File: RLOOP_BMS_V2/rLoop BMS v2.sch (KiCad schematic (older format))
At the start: 0 parts

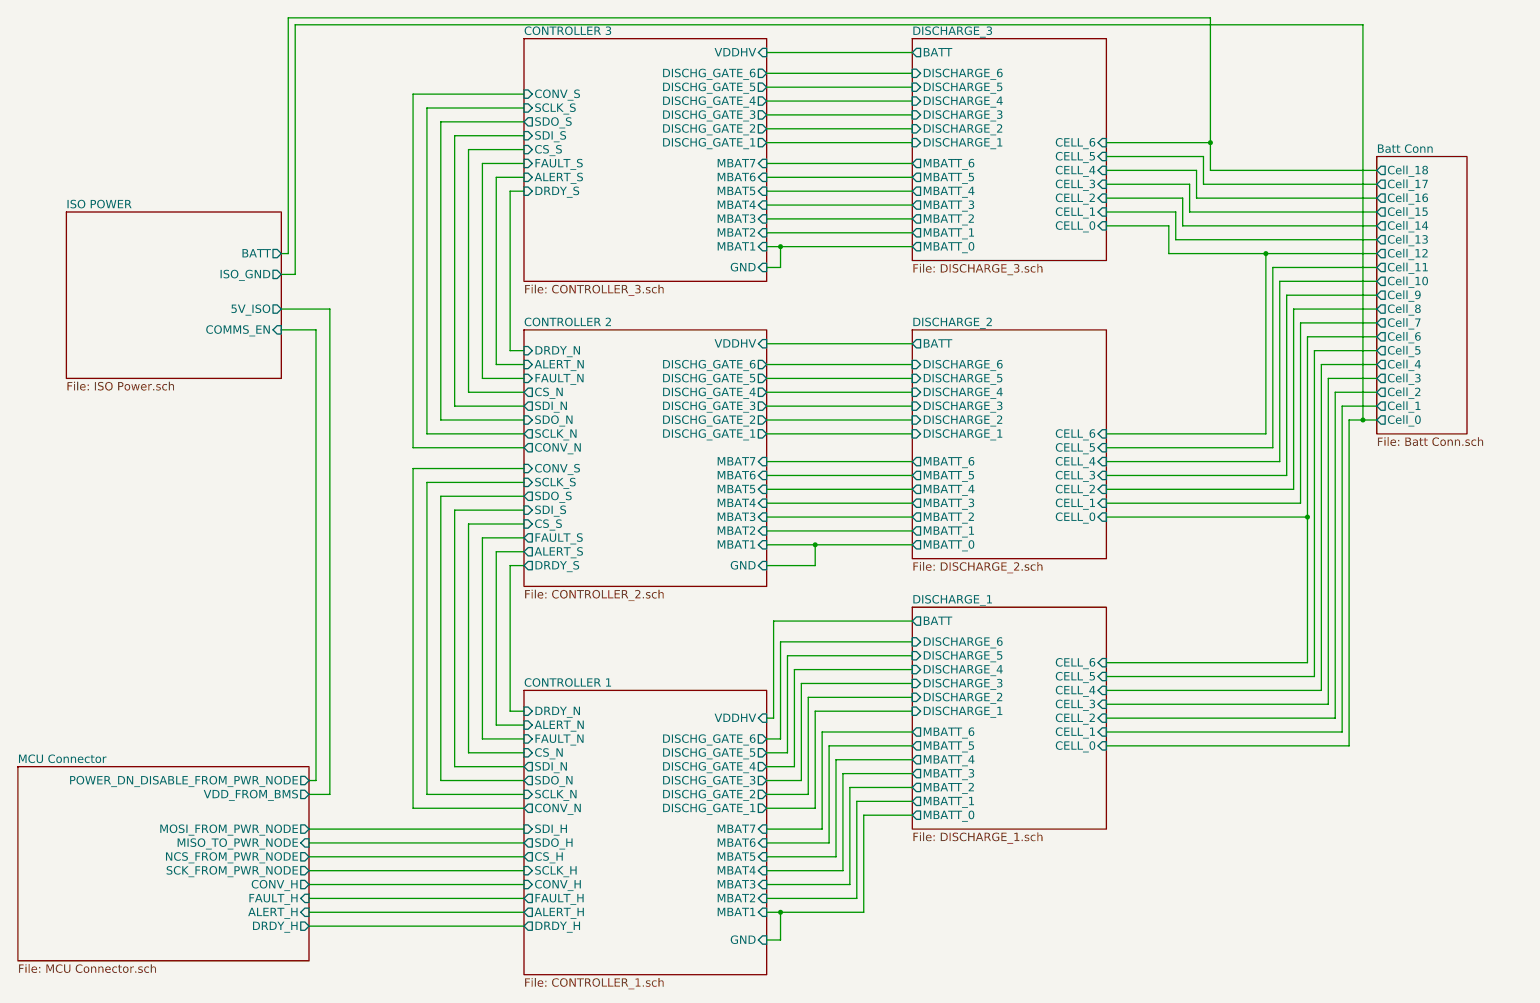
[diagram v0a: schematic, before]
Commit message: Updated page sizes for schematics
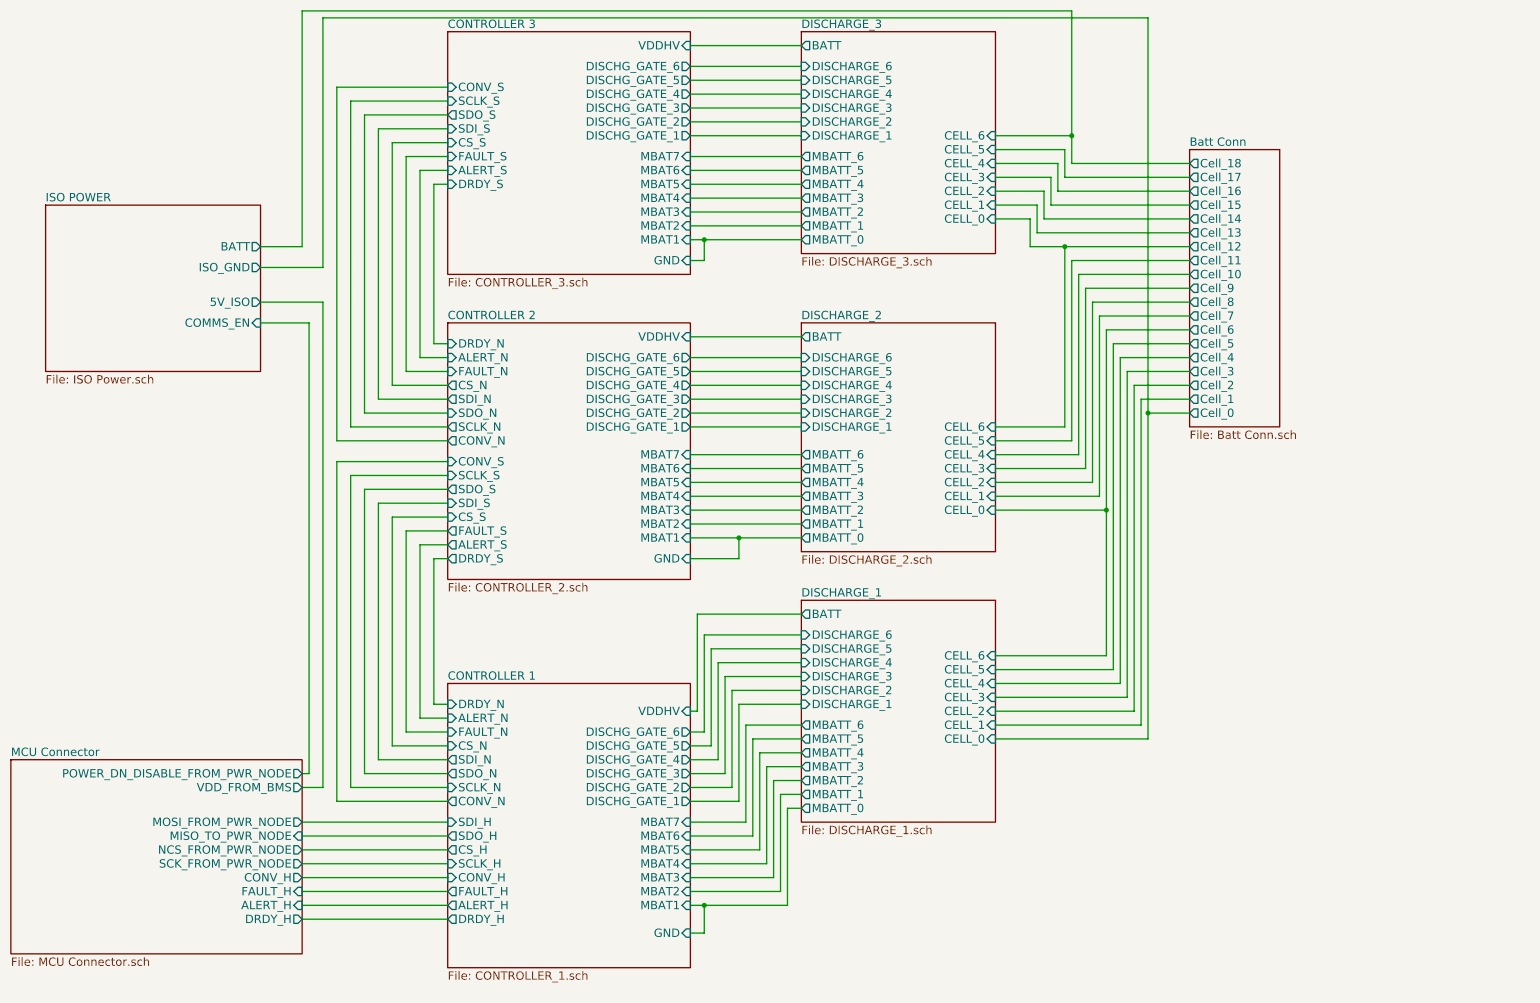
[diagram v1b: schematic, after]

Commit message: change Q1 transistor
Fixing something out of stock
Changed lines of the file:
@@
 	5450 2050 6250 2050
 Wire Wire Line
-	5450 2150 5550 2150
-Wire Wire Line
-	5550 2150 6250 2150
+	5450 2150 6250 2150
 Wire Wire Line
 	5450 2300 5550 2300
@@
 	5450 4200 6250 4200
 Wire Wire Line
-	5450 4300 5800 4300
-Wire Wire Line
-	5800 4300 6250 4300
+	5450 4300 6250 4300
 Wire Wire Line
 	5450 5550 5500 5550
@@
 	6150 6950 6150 6250
 Wire Wire Line
-	5450 6950 5550 6950
-Wire Wire Line
-	5550 6950 6150 6950
+	5450 6950 6150 6950
 Wire Wire Line
 	5450 7150 5550 7150
@@
 Connection ~ 5550 6950
 Wire Wire Line
-	8750 550  8750 3400
-Wire Wire Line
-	8750 3400 8750 5750
+	8750 550  8750 5750
 Wire Wire Line
 	8750 5750 7650 5750
@@
 	8450 5150 7650 5150
 Wire Wire Line
-	8450 2800 8450 4100
-Wire Wire Line
-	8450 4100 8450 5150
+	8450 2800 8450 5150
 Wire Wire Line
 	8450 2800 9050 2800
@@
 	8200 2300 9050 2300
 Wire Wire Line
-	7900 2200 8150 2200
-Wire Wire Line
-	8150 2200 9050 2200
+	7900 2200 9050 2200
 Wire Wire Line
 	8150 2200 8150 3500
@@
 	8200 1600 9050 1600
 Wire Wire Line
-	8200 500  8200 1400
-Wire Wire Line
-	8200 1400 8200 1600
+	8200 500  8200 1600
 Wire Wire Line
 	8200 1400 7650 1400

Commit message: swapped a few connectors to standardize with the power node and what's readily available
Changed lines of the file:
@@
 	6250 6250 6150 6250
 Wire Wire Line
-	6150 6950 6150 6250
+	6150 6250 6150 6950
 Wire Wire Line
-	5450 6950 6150 6950
+	6150 6950 5450 6950
 Wire Wire Line
 	5450 7150 5550 7150
